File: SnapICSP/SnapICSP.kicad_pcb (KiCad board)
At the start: 2 copper layers, 20.3 x 25.4 mm, 3 parts, among them J1 Conn_01x08_Male, J2 AVR-ISP-6, J3 AVR-ISP-6

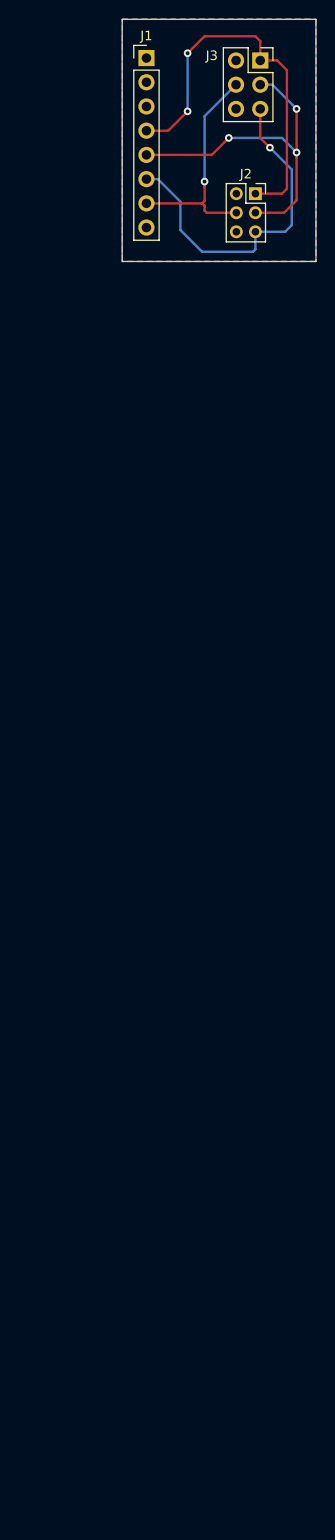
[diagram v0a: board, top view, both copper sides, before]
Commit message: Corrected pinout on component
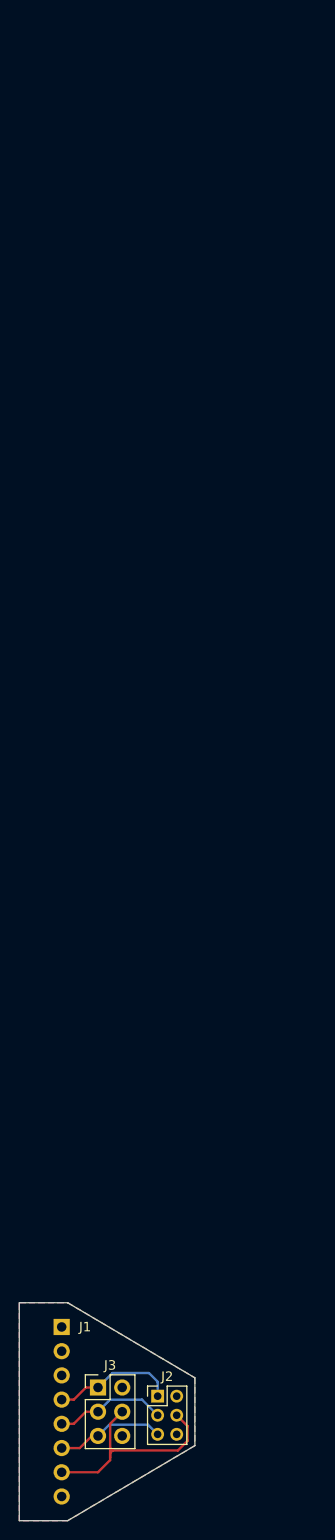
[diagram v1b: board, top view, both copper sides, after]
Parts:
- J1: footprint Socket_Strips:Socket_Strip_Straight_1x08_Pitch2.54mm -> Pin_Headers:Pin_Header_Angled_1x08_Pitch2.54mm; moved to B.Cu
- J2: footprint Socket_Strips:Socket_Strip_Straight_2x03_Pitch2.00mm -> Pin_Headers:Pin_Header_Straight_2x03_Pitch2.00mm
- J3: footprint Socket_Strips:Socket_Strip_Straight_2x03_Pitch2.54mm -> Pin_Headers:Pin_Header_Straight_2x03_Pitch2.54mm
- moved J3 140.2 mm to (83.8, 85.1)
- moved J1 133.4 mm to (80.0, 78.7), turned to 180 degrees
- moved J2 126.5 mm to (90.1, 86.0)
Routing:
- net Net-(J1-Pad4): track 41.0 -> 13.1 mm, vias 2 -> 0
- net Net-(J1-Pad5): track 36.4 -> 11.8 mm, vias 3 -> 0
- net Net-(J1-Pad6): track 35.9 -> 11.5 mm, vias 1 -> 0
- net Net-(J1-Pad7): track 24.1 -> 23.9 mm, vias 1 -> 0
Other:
- board size 20.3 x 25.4 mm -> 18.4 x 22.9 mm
